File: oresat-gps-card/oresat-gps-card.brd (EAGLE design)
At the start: 99.8 x 94.6 mm, 374 parts, among them J1 ORESAT-DEBUG-CONNECTOR-CARD, J100 DM3BT-DSF-PEJS, J102 FTSH-105-XX-X-DV-K, J4 TFM-120-01-L-D-RA, Q1 MMBT2907, Q2 PMV45EN, Q3 DMP2240UDM, Q4 PMV45EN, Q5 MOSFET-PCH-SOT23-6, Q6 MOSFET-PCH-SOT23-6, U1 RCLAMP0504FB, U10 TLVH431, U11 TCAN330, U12 MIC842LYC5, U13 MIC842LYC5, U14 MAX4211FETE, U15 TPS62112, U16 MAX7310ATE, U17 25AAXX, U18 RCLAMP0504FB, U19 BP2G+, U2 TPS2051CDBVR, U20 MAX8510EXK29+T, U22 LT1719S6, U4 SN74LVC1G07DCK, U5 SKY65723-81, U6 7Q-16.368MBG-T, U7 OSD3358-512M-BSM, U8 MAX8510EXK29+T, U9 MAX8510EXK29+T, Y1 24MHz, Y2 ABS07-32.768KHZ-T

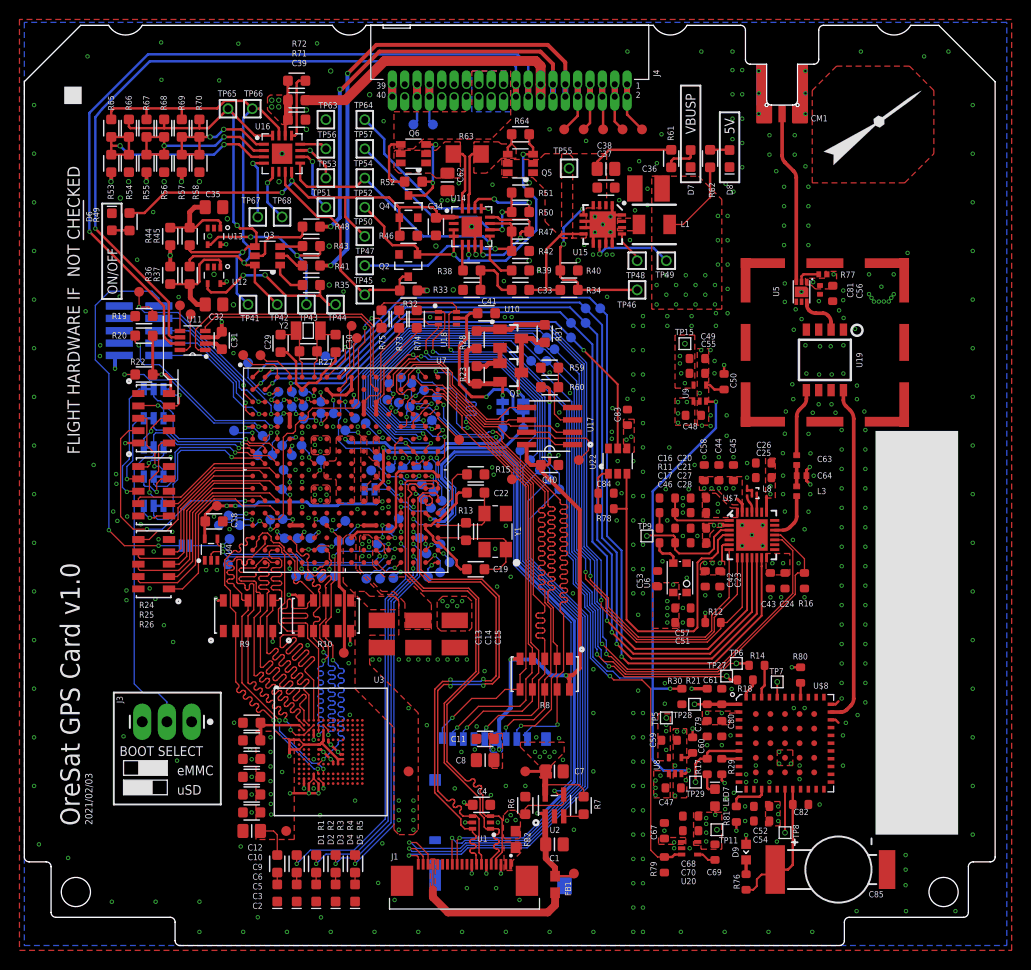
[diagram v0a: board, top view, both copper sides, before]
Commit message: Fixed design review things: made net names more clear, removed solder mask from top of RF traces, opened up space around octavo 3.3v pads, moved digital LDO for the max chip, added pin header and through hole testpoints for GPS lines. Some other small changes.
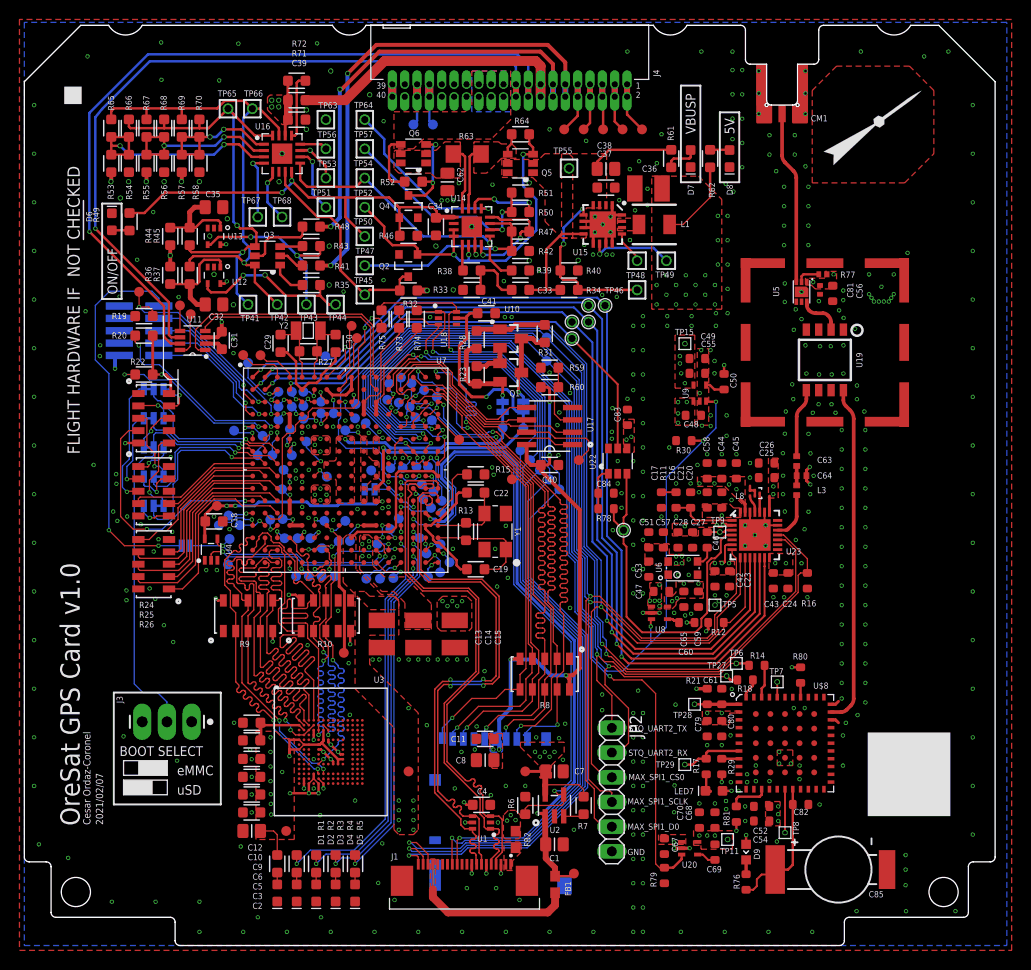
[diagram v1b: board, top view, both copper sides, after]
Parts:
- removed TP10, TP143, TP36, TP37: TEST-POINT3X4, SparkFun-Connectors:PAD.03X.04
- removed U$7: MAX2771ETI+, U-Maxim-MAX2771-Multiband-Universal-GNSS-Receiver:90-0023
- added C65: 100n, oresat-rcl:.0603-B-NOSILK
- added JP2: (no value), pinhead:1X06
- added TP72: TEST-POINT-LARGE-SQUARE, oresat-misc:1X01
- added U23: MAX2771ETI+, U-Maxim-MAX2771-Multiband-Universal-GNSS-Receiver:90-0023
- TP20, TP21, TP33, TP34, TP71: value TEST-POINT3X4 -> TEST-POINT-LARGE-SQUARE; device SparkFun-Connectors:PAD.03X.04 -> oresat-misc:1X01
- U3: value (none) -> THGBMJG7C2LBAU8
- moved R30 26.3 mm to (67.8, 51.9), turned to 0 degrees
- moved TP71 20.5 mm to (61.6, 42.7), flipped to the top
- moved C47 20.2 mm to (65.5, 36.4)
- moved U8 15.8 mm to (65.3, 34.2), turned to 270 degrees
- moved C59 14.8 mm to (69.3, 35.6), turned to 270 degrees
- moved TP5 12.6 mm to (71.0, 35.0)
- moved C60 12.6 mm to (68.1, 33.2), turned to 180 degrees
- moved C51 9.19 mm to (64.2, 41.7), turned to 90 degrees
- moved TP9 7.51 mm to (71.5, 42.5)
- moved C57 7.28 mm to (65.7, 41.7), turned to 90 degrees
- moved C46 4.11 mm to (70.2, 41.7), turned to 90 degrees
- moved C17 2.96 mm to (65.5, 45.8), turned to 270 degrees
- moved C68 2.53 mm to (71.0, 12.9), turned to 90 degrees
- moved C16 2.41 mm to (68.5, 45.8), turned to 90 degrees
- moved C20 2.41 mm to (71.7, 45.8), turned to 90 degrees
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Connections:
- removed net SPI1_CS0: R12.1, TP143.P$1, U$7.9, U7.J14
- removed net SPI1_D0: TP36.P$1, U$7.7, U7.F14
- removed net SPI1_SCLK: TP37.P$1, U$7.8, U7.F15
- removed net UART2_RX: R18.1, TP147.P$1, TP27.P$1, U7.H16
- removed net UART2_TX: R14.1, TP10.P$1, TP6.P$1, U7.E16
- new net MAX_SPI1_CS0: JP2.3, R12.1, U23.9, U7.J14
- new net MAX_SPI1_D0: JP2.5, U23.7, U7.F14
- new net MAX_SPI1_SCLK: JP2.4, U23.8, U7.F15
- new net STQ_UART2_RX: JP2.2, R18.1, TP147.P$1, TP27.P$1, U7.H16
- new net STQ_UART2_TX: JP2.1, R14.1, TP6.P$1, U7.E16
- net 2.85VA: now also U23.2, U23.22, U23.27, U23.28; no longer U$7.2, U$7.22, U$7.27, U$7.28
- net 2.85VD: now also C65.1, U23.14, U23.6; no longer U$7.14, U$7.6
- net CPOUT: now also U23.1; no longer U$7.1
- net GND: now also C65.2, JP2.6, U23.20, U23.23, U23.26, U23.BODY; no longer U$7.BODY
- net I0: now also TP20.1, U23.12; no longer TP21.P$1, U$7.12
- net I1: now also TP21.1, U23.13; no longer TP20.P$1, U$7.13
- net LNAOUT: now also U23.24; no longer U$7.24
- net MAX-CLKOUT: now also TP72.1; no longer TP71.P$1
- net MAX_!SHDN: now also U23.18; no longer U$7.18
- net MAX_CLK_OUT: now also TP71.1, U23.4; no longer U$7.4
- net MAX_LD: now also U23.17; no longer U$7.17
- net MIXIN: now also U23.25; no longer U$7.25
- net N$124: now also U23.19; no longer U$7.19
- net Q0: now also TP33.1, U23.11; no longer TP34.P$1, U$7.11
- net Q1: now also TP34.1, U23.10; no longer TP33.P$1, U$7.10
- net XTAL: now also U23.3; no longer U$7.3
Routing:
- net MAX_SPI1_CS0: track 0.00 -> 114.9 mm, vias 0 -> 2
- net MAX_SPI1_D0: track 0.00 -> 108.6 mm, vias 0 -> 2
- net MAX_SPI1_SCLK: track 0.00 -> 104.3 mm, vias 0 -> 2
- net SPI1_CS0: track 94.7 -> 0.00 mm, vias 2 -> 0
- net STQ_UART2_RX: track 0.00 -> 94.1 mm, vias 0 -> 2
- net STQ_UART2_TX: track 0.00 -> 86.9 mm, vias 0 -> 2
- net UART2_RX: track 83.0 -> 0.00 mm, vias 2 -> 0
- net SPI1_D0: track 82.2 -> 0.00 mm, vias 2 -> 0
- net SPI1_SCLK: track 81.1 -> 0.00 mm, vias 2 -> 0
- net UART2_TX: track 78.7 -> 0.00 mm, vias 2 -> 0
- net MAX-EN: track 117.9 -> 102.7 mm
- net XTAL: track 11.7 -> 2.64 mm
- net GND: track 36.1 -> 43.6 mm, vias 508 -> 510
- net 2.85V-S: track 7.97 -> 5.73 mm, vias 18 -> 19
- net STQ-EN: track 86.2 -> 88.3 mm
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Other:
- board text added: "2021/02/07"
- board text added: "Cesar Ordaz-Coronel"
- board text added: "GND"
- board text added: "MAX_SPI1_CS0"
- board text added: "MAX_SPI1_D0"
- board text added: "MAX_SPI1_SCLK"
- board text added: "STQ_UART2_RX"
- board text added: "STQ_UART2_TX"
- board text removed: "2021/02/03"

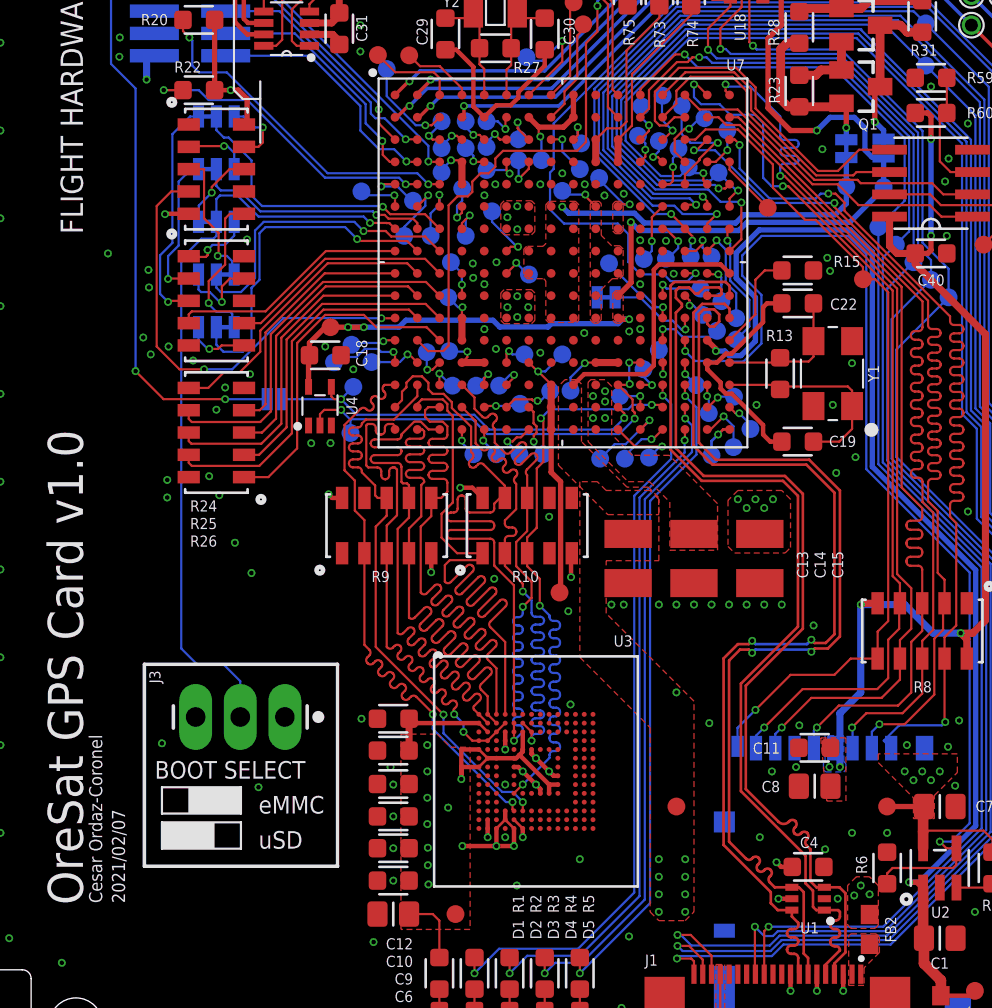
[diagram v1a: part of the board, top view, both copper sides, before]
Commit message: Fixed 3.3VA rail for I2C protection chip.
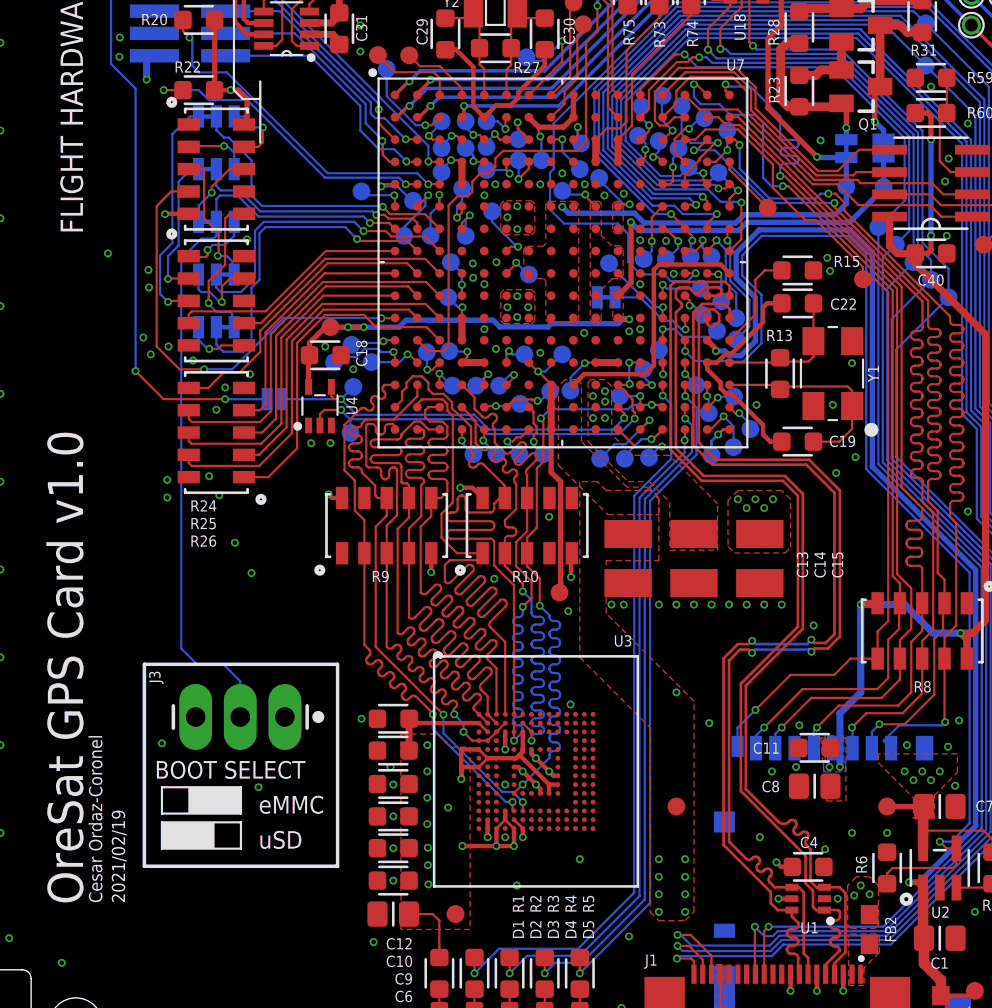
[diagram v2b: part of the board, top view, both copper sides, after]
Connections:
- removed net N$26: JP101.1, TP165.P$1, U7.F8, U7.F9, U7.G8, U7.G9, U7.H7, U7.H8, U7.H9, U7.J7, U7.J8, U7.J9, U7.K8, U7.K9, U7.L8, U7.L9
- new net N$133: C18.1, JP104.1, TP14.P$1, TP164.P$1, U4.5, U7.K11, U7.L11
- net 3.3VA: now also JP101.1, TP165.P$1, U7.F8, U7.F9, U7.G8, U7.G9, U7.H7, U7.H8, U7.H9, U7.J7, U7.J8, U7.J9, U7.K8, U7.K9, U7.L8, U7.L9; no longer C18.1, JP104.1, TP14.P$1, TP164.P$1, U4.5, U7.K11, U7.L11
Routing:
- net N$133: track 0.00 -> 45.1 mm, vias 0 -> 4
- net 3.3VA: track 63.7 -> 34.9 mm, vias 5 -> 2
- net N$26: track 19.6 -> 0.00 mm, vias 1 -> 0
- added copper zone on layer 1, net N$133
- removed copper zone on layer 1, net N$26
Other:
- board text added: "2021/02/19"
- board text removed: "2021/02/07"

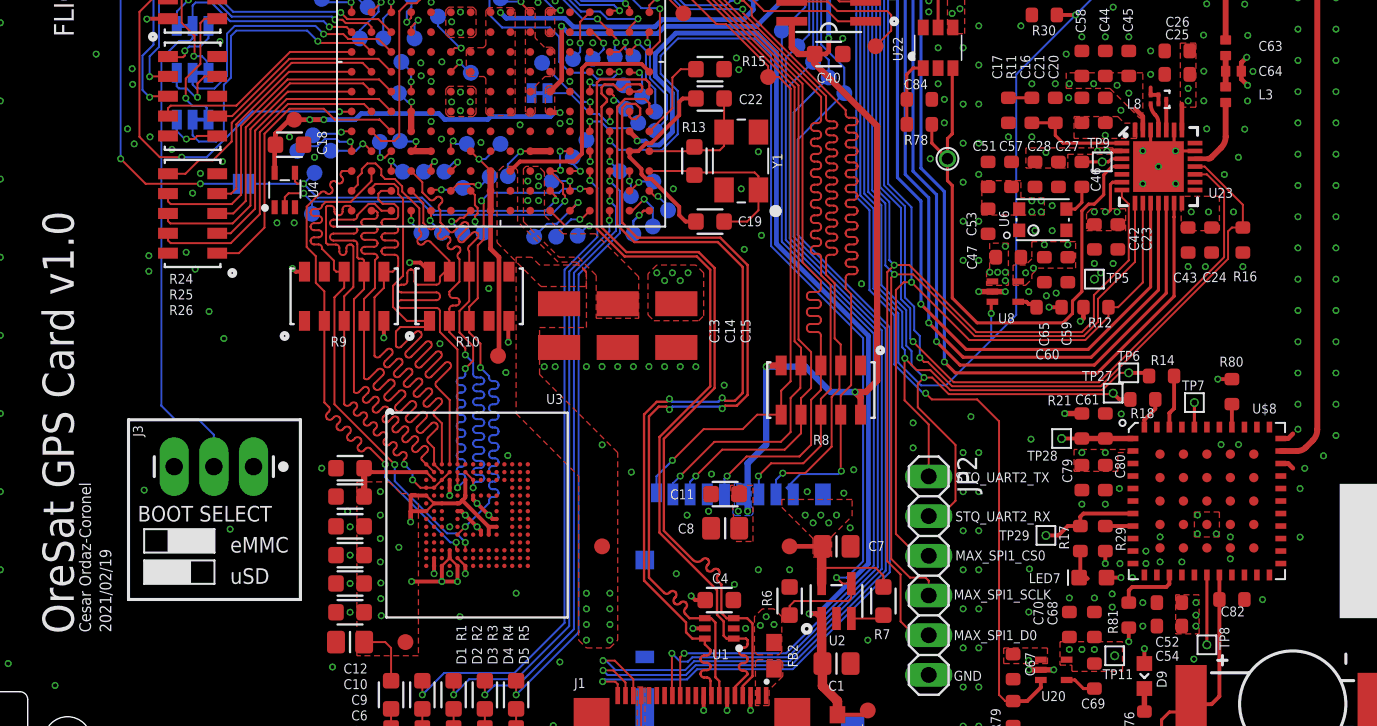
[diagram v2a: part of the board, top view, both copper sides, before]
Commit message: Added attributes to some parts, and changed internal cutout polygons to 0.1 width instead of 0 width.
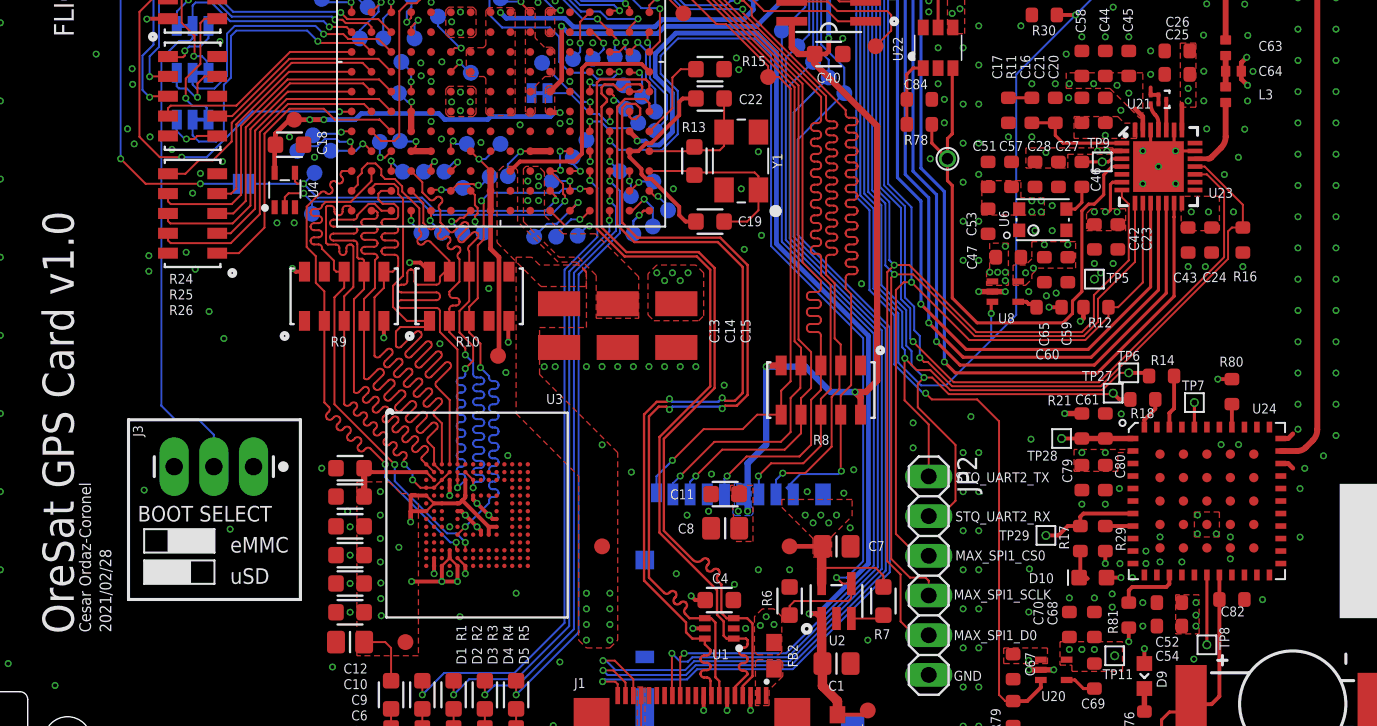
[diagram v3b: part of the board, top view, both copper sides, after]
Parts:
- renumbered L8 to U21, LED7 to D10, U$8 to U24
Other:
- board text added: "2021/02/28"
- board text removed: "2021/02/19"

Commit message: Updated oscillator capacitor values and added BOM
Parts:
- C19, C22, C29, C30: value 18pF, 50V -> 12pF, 50V
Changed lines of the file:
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@@
 </element>
 <element name="TP14" library="SparkFun-Connectors" package="PAD.03X.04" package3d_urn="urn:adsk.eagle:package:38287/1" value="TEST-POINT3X4" x="19.8" y="45.2" smashed="yes" rot="R90"/>
-<element name="C22" library="oresat-rcl" package=".0603-A" value="18pF, 50V" x="46.40625" y="46.55625" smashed="yes">
+<element name="C22" library="oresat-rcl" package=".0603-A" value="12pF, 50V" x="46.40625" y="46.55625" smashed="yes">
 <attribute name="NAME" x="48.25625" y="46.19375" size="0.635" layer="25" font="vector" ratio="20"/>
 <attribute name="NAME" x="46.40625" y="46.55625" size="0.3" layer="33" ratio="15" align="center"/>
 <attribute name="VALUE" x="45.00625" y="44.80625" size="0.8" layer="27" font="vector" ratio="15"/>
 </element>
-<element name="C19" library="oresat-rcl" package=".0603-A" value="18pF, 50V" x="46.40625" y="38.68125" smashed="yes">
+<element name="C19" library="oresat-rcl" package=".0603-A" value="12pF, 50V" x="46.40625" y="38.68125" smashed="yes">
 <attribute name="NAME" x="48.19375" y="38.38125" size="0.635" layer="25" font="vector" ratio="20"/>
 <attribute name="NAME" x="46.40625" y="38.68125" size="0.3" layer="33" ratio="15" align="center"/>
@@
 <attribute name="DPN" value="THGBMJG7C2LBAU8-ND" x="31.5" y="19.9" size="1.778" layer="27" display="off"/>
 <attribute name="MPN" value="THGBMJG7C2LBAU8" x="31.5" y="19.9" size="1.778" layer="27" display="off"/>
+<attribute name="NAME" x="35.925" y="27.0125" size="0.635" layer="25" font="vector" ratio="20"/>
 <attribute name="NAME" x="31.5" y="19.9" size="1.5" layer="33" ratio="15" align="center"/>
-<attribute name="NAME" x="35.925" y="27.0125" size="0.635" layer="25" font="vector" ratio="20"/>
 <attribute name="VALUE" x="25.9" y="12.3" size="0.8" layer="27" font="vector" ratio="15"/>
 </element>
@@
 <attribute name="VALUE" x="27.7875" y="59.3375" size="0.8" layer="27" font="vector" ratio="15"/>
 </element>
-<element name="C30" library="oresat-rcl" package=".0603-A" value="18pF, 50V" x="32" y="61.9" smashed="yes" rot="R270">
+<element name="C30" library="oresat-rcl" package=".0603-A" value="12pF, 50V" x="32" y="61.9" smashed="yes" rot="R270">
 <attribute name="NAME" x="33.075" y="62.83125" size="0.635" layer="25" font="vector" ratio="20" rot="R270"/>
 <attribute name="NAME" x="32" y="61.9" size="0.3" layer="33" ratio="15" rot="R270" align="center"/>
 <attribute name="VALUE" x="30.25" y="63.3" size="0.8" layer="27" font="vector" ratio="15" rot="R270"/>
 </element>
-<element name="C29" library="oresat-rcl" package=".0603-A" value="18pF, 50V" x="26.34375" y="61.9" smashed="yes" rot="R270">
+<element name="C29" library="oresat-rcl" package=".0603-A" value="12pF, 50V" x="26.34375" y="61.9" smashed="yes" rot="R270">
 <attribute name="NAME" x="24.7" y="62.8" size="0.635" layer="25" font="vector" ratio="20" rot="R270"/>
 <attribute name="NAME" x="26.34375" y="61.9" size="0.3" layer="33" ratio="15" rot="R270" align="center"/>
